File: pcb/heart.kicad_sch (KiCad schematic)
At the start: 44 parts, among them SW1 Power, SW2 Button, U1 74AHC595, U2 74AHC595, U3 MSP430G2533IN20, U4 BST

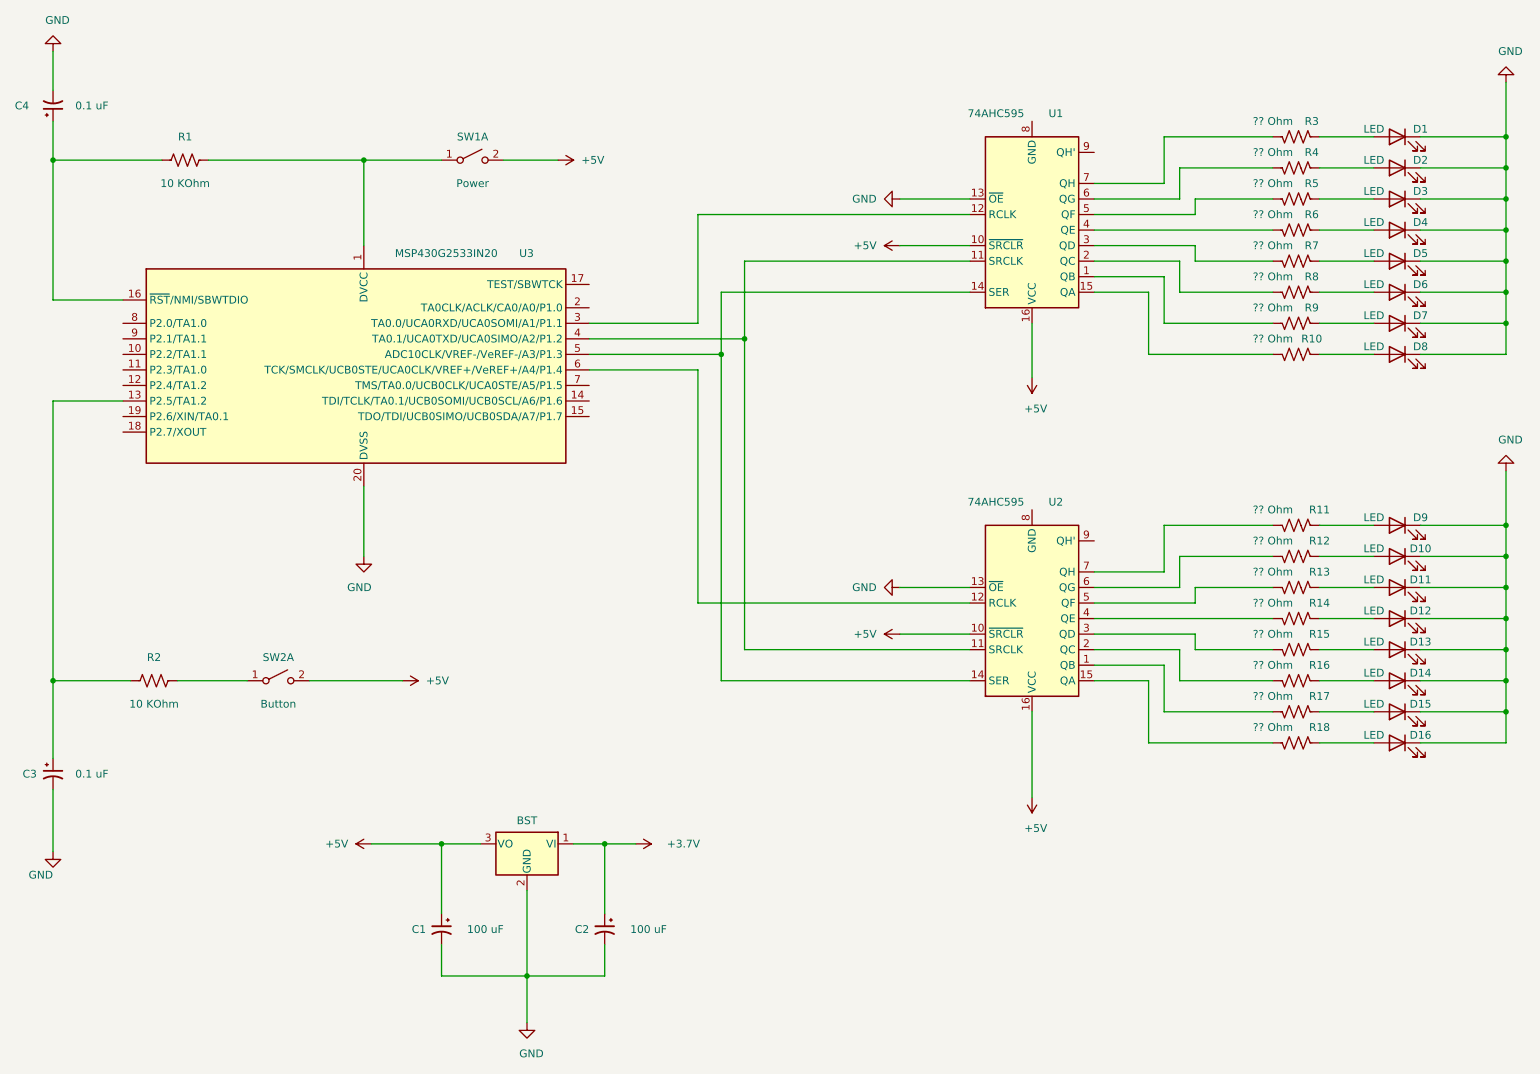
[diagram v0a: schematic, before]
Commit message: Move pcb files one folder up
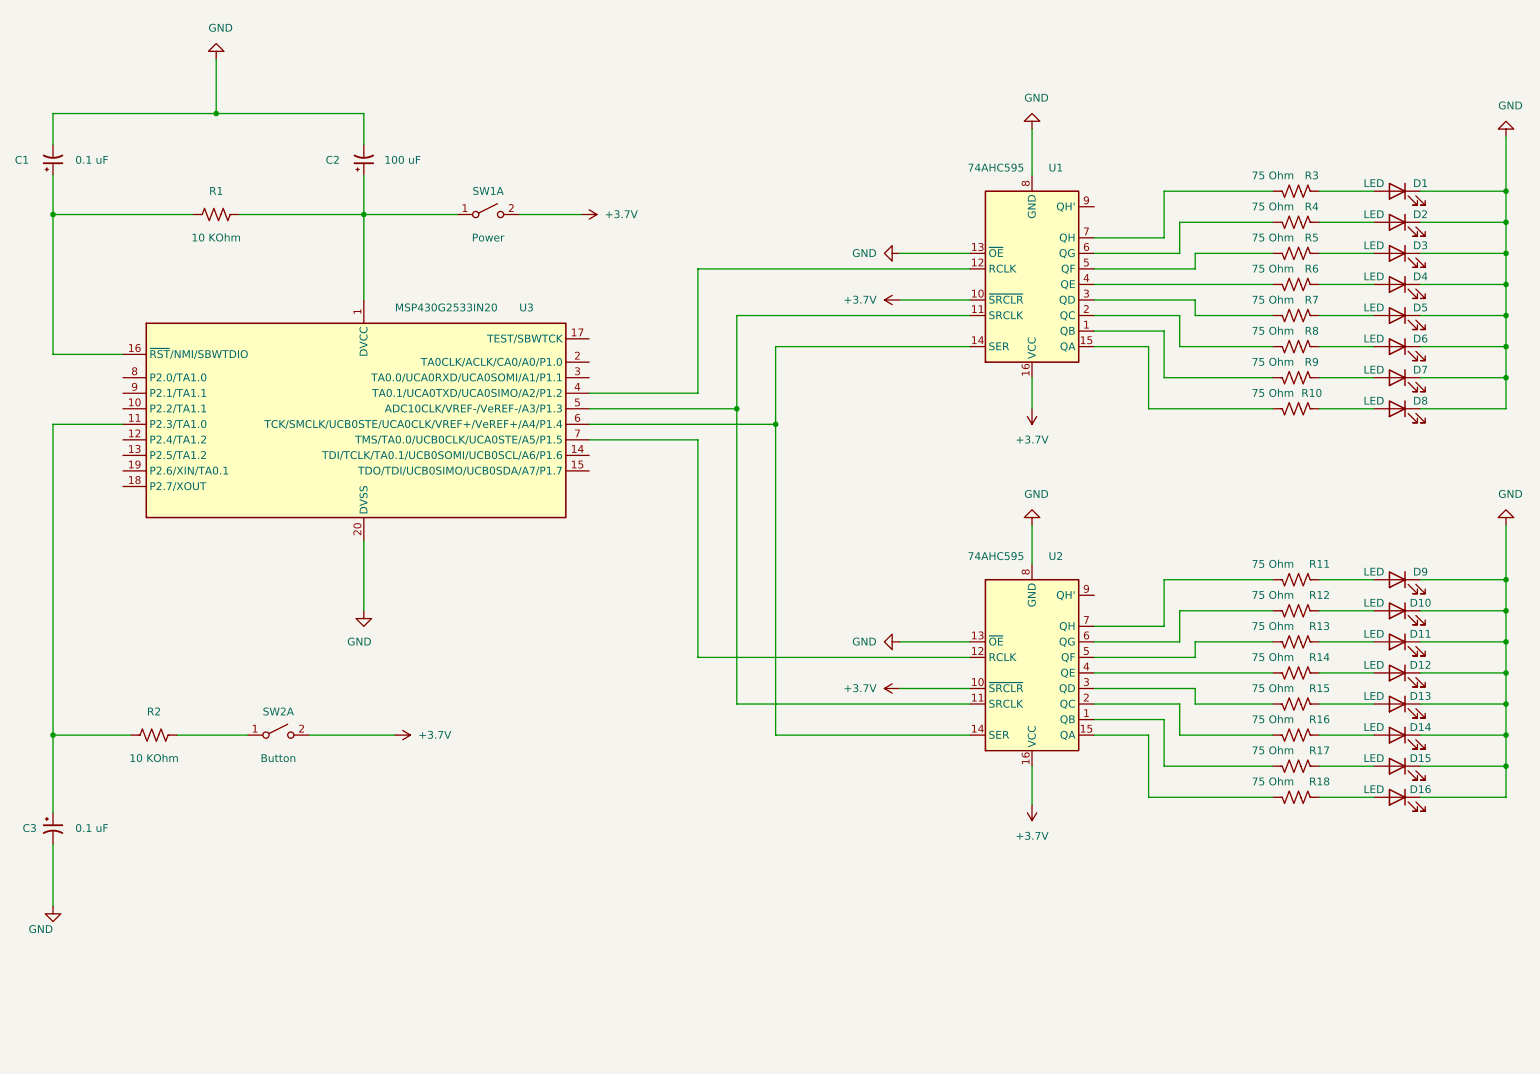
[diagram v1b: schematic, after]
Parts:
- removed C1: 100 uF, symbol Device:C_Polarized_Small_US
- removed U4: BST, Package_TO_SOT_THT:TO-220-3_Vertical, symbol Regulator_Linear:SPX2920U-5.0_TO220
- R10, R11, R12, R13, R14, R15, R16, R17, R18, R3, R4, R5, R6, R7, R8, R9: value ?? Ohm -> 75 Ohm
- renumbered C4 to C1
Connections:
- net +3.7V is gone; now on an unnamed net: C2.1
- net GND: now also U1.8 (GND), U2.8 (GND)
- net at C3.1, R2.2: now also U3.11 (P2.3/TA1.0); no longer U3.13 (P2.5/TA1.2)
- net at U1.11 (SRCLK), U2.11 (SRCLK): now also U3.5 (ADC10CLK/VREF-/VeREF-/A3/P1.3); no longer U3.4 (TA0.1/UCA0TXD/UCA0SIMO/A2/P1.2)
- net at U2.12 (RCLK): now also U3.7 (TMS/TA0.0/UCB0CLK/UCA0STE/A5/P1.5); no longer U3.6 (TCK/SMCLK/UCB0STE/UCA0CLK/VREF+/VeREF+/A4/P1.4)
- net at U1.14 (SER), U2.14 (SER): now also U3.6 (TCK/SMCLK/UCB0STE/UCA0CLK/VREF+/VeREF+/A4/P1.4); no longer U3.5 (ADC10CLK/VREF-/VeREF-/A3/P1.3)
- net at U1.12 (RCLK): now also U3.4 (TA0.1/UCA0TXD/UCA0SIMO/A2/P1.2); no longer U3.3 (TA0.0/UCA0RXD/UCA0SOMI/A1/P1.1)
- net +5V renamed +3.3VDAC
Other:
- company: (none) -> Maksym Dybarskyi
- title: (none) -> Heart LEDs
- moved on the sheet: C1, C3, D1, D10, D11, D12, D13, D14, D15, D16, D2, D3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
